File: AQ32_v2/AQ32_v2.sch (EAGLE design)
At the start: 114 parts, among them Q2 BCV27, Q3 BCV27, Q5 BCV27, Q6 BCV27, U1 ITG-3200, U10 MS5611, U11 MIC5239, U13 74AHC1G86DCK, U2 STM32F10XVXT6, U7 USD-SOCKETNEW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

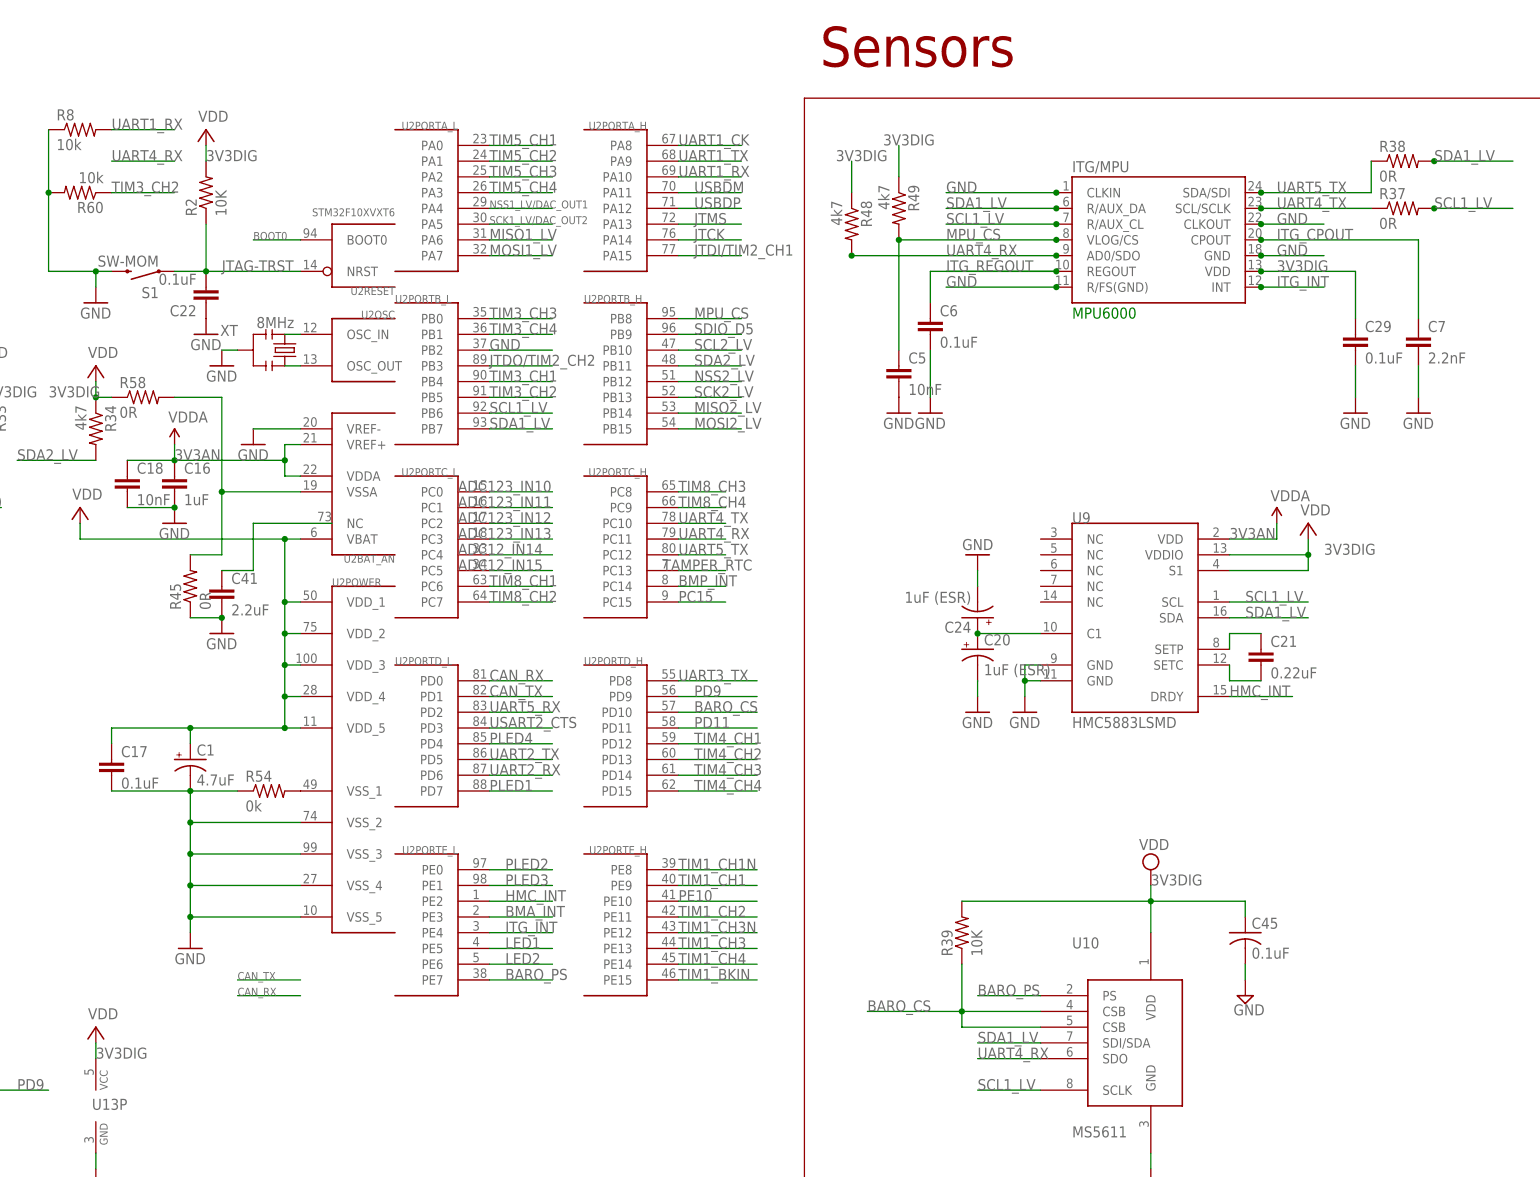
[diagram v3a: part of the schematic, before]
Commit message: converted baro back to using I2C, renamed TX4/TX5 to use I2C3 labels
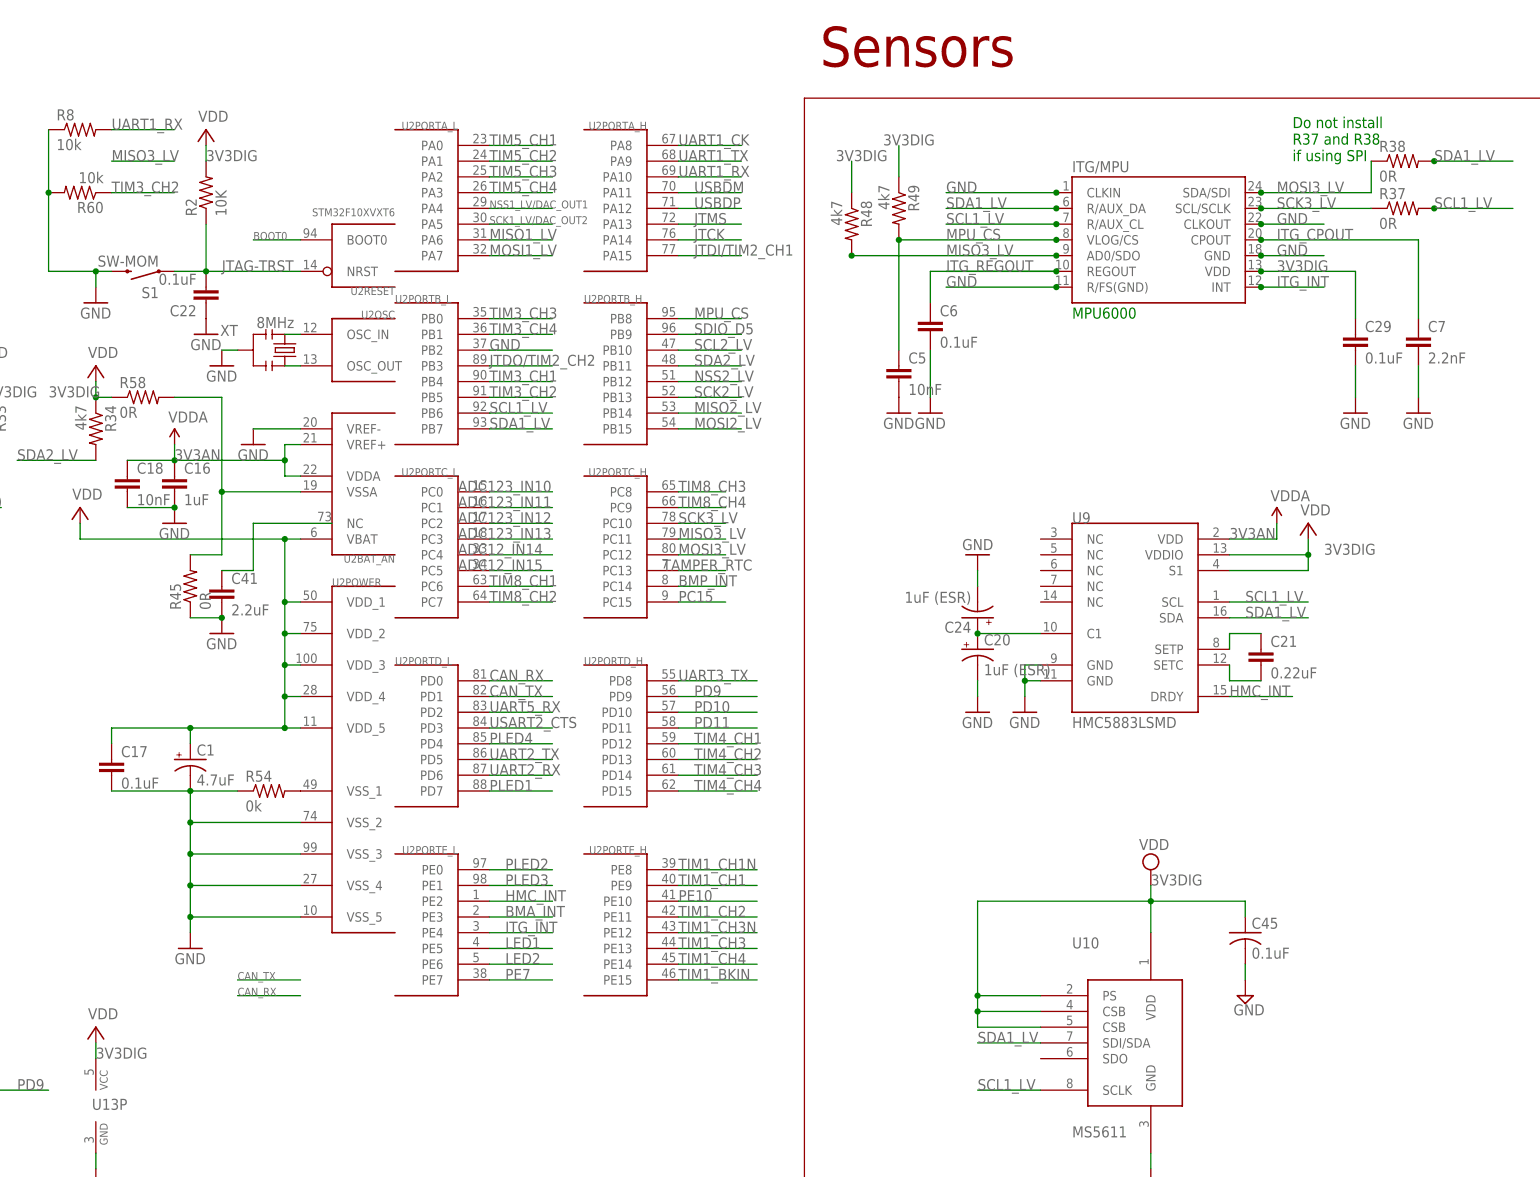
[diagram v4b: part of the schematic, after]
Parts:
- removed R39: 10K, SparkFun:RESISTOR0402
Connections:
- net UART4_TX renamed SCK3_LV
- net UART5_TX renamed MOSI3_LV
- removed net BARO_CS: R39.1, U10.CSB, U10.CSB@2, U2PORTD_H.PD10
- removed net BARO_PS: U10.PS, U2PORTE_L.PE7
- removed net UART4_RX: R48.2, U1.AD0/SDO, U10.SDO, U2PORTC_H.PC11
- new net MISO3_LV: R48.2, U1.AD0/SDO, U2PORTC_H.PC11
- new net PD10: U2PORTD_H.PD10
- new net PE7: U2PORTE_L.PE7
- net 3V3DIG: now also U10.CSB, U10.CSB@2, U10.PS; no longer R39.2
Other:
- note added: "Do not install R37 and R38 if using SPI"
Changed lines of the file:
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@@
 <part name="JP3-1" library="SparkFun-Connectors" deviceset="M09" device=""/>
 <part name="JP3-2" library="SparkFun-Connectors" deviceset="M09" device=""/>
-<part name="R39" library="SparkFun" deviceset="RESISTOR" device="0402" value="10K"/>
 <part name="JP5" library="SparkFun-Connectors" deviceset="M02" device="PTH"/>
 </parts>
@@
 <text x="500.38" y="73.66" size="1.778" layer="91">AI4</text>
 <text x="500.38" y="76.2" size="1.778" layer="91">AI5</text>
+<text x="332.74" y="175.26" size="1.778" layer="91">Do not install
+R37 and R38
+if using SPI</text>
 </plain>
 <instances>
@@
 <instance part="JP3-1" gate="G$1" x="447.04" y="68.58"/>
 <instance part="JP3-2" gate="G$1" x="472.44" y="68.58"/>
-<instance part="R39" gate="G$1" x="279.4" y="50.8" rot="R90"/>
 <instance part="JP5" gate="G$1" x="114.3" y="-43.18"/>
 </instances>
@@
 <wire x1="309.88" y1="58.42" x2="309.88" y2="55.88" width="0.1524" layer="91"/>
 <wire x1="309.88" y1="55.88" x2="309.88" y2="50.8" width="0.1524" layer="91"/>
-<wire x1="279.4" y1="55.88" x2="309.88" y2="55.88" width="0.1524" layer="91"/>
 <wire x1="309.88" y1="55.88" x2="325.12" y2="55.88" width="0.1524" layer="91"/>
 <wire x1="325.12" y1="55.88" x2="325.12" y2="53.34" width="0.1524" layer="91"/>
@@
 <pinref part="C45" gate="G$1" pin="1"/>
 <label x="309.88" y="58.42" size="1.778" layer="95"/>
-<pinref part="R39" gate="G$1" pin="2"/>
+<wire x1="309.88" y1="55.88" x2="281.94" y2="55.88" width="0.1524" layer="91"/>
+<wire x1="281.94" y1="55.88" x2="281.94" y2="40.64" width="0.1524" layer="91"/>
+<pinref part="U10" gate="G$1" pin="CSB@2"/>
+<wire x1="281.94" y1="40.64" x2="281.94" y2="38.1" width="0.1524" layer="91"/>
+<wire x1="281.94" y1="38.1" x2="281.94" y2="35.56" width="0.1524" layer="91"/>
+<wire x1="281.94" y1="35.56" x2="292.1" y2="35.56" width="0.1524" layer="91"/>
+<pinref part="U10" gate="G$1" pin="CSB"/>
+<wire x1="292.1" y1="38.1" x2="281.94" y2="38.1" width="0.1524" layer="91"/>
+<pinref part="U10" gate="G$1" pin="PS"/>
+<wire x1="292.1" y1="40.64" x2="281.94" y2="40.64" width="0.1524" layer="91"/>
+<junction x="281.94" y="40.64"/>
+<junction x="281.94" y="38.1"/>
 </segment>
 <segment>
@@
 </segment>
 </net>
-<net name="UART4_TX" class="0">
+<net name="SCK3_LV" class="0">
 <segment>
 <wire x1="233.68" y1="116.84" x2="241.3" y2="116.84" width="0.1524" layer="91"/>
@@
 </segment>
 </net>
-<net name="UART4_RX" class="0">
+<net name="MISO3_LV" class="0">
 <segment>
 <wire x1="233.68" y1="114.3" x2="241.3" y2="114.3" width="0.1524" layer="91"/>
@@
 <pinref part="U1" gate="G$1" pin="AD0/SDO"/>
 <pinref part="R48" gate="G$1" pin="2"/>
-</segment>
-<segment>
-<pinref part="U10" gate="G$1" pin="SDO"/>
-<wire x1="292.1" y1="30.48" x2="281.94" y2="30.48" width="0.1524" layer="91"/>
-<label x="281.94" y="30.48" size="1.778" layer="95"/>
 </segment>
 </net>
@@
 </segment>
 </net>
-<net name="UART5_TX" class="0">
+<net name="MOSI3_LV" class="0">
 <segment>
 <wire x1="233.68" y1="111.76" x2="241.3" y2="111.76" width="0.1524" layer="91"/>
@@
 </segment>
 </net>
-<net name="BARO_CS" class="0">
+<net name="PD10" class="0">
 <segment>
 <wire x1="233.68" y1="86.36" x2="246.38" y2="86.36" width="0.1524" layer="91"/>
 <label x="236.22" y="86.36" size="1.778" layer="95"/>
 <pinref part="U2" gate="PORTD_H" pin="PD10"/>
-</segment>
-<segment>
-<pinref part="U10" gate="G$1" pin="CSB@2"/>
-<wire x1="292.1" y1="35.56" x2="279.4" y2="35.56" width="0.1524" layer="91"/>
-<pinref part="R39" gate="G$1" pin="1"/>
-<wire x1="279.4" y1="35.56" x2="279.4" y2="38.1" width="0.1524" layer="91"/>
-<pinref part="U10" gate="G$1" pin="CSB"/>
-<wire x1="279.4" y1="38.1" x2="279.4" y2="45.72" width="0.1524" layer="91"/>
-<wire x1="292.1" y1="38.1" x2="279.4" y2="38.1" width="0.1524" layer="91"/>
-<junction x="279.4" y="38.1"/>
-<wire x1="279.4" y1="38.1" x2="264.16" y2="38.1" width="0.1524" layer="91"/>
-<label x="264.16" y="38.1" size="1.778" layer="95"/>
 </segment>
 </net>
@@
 </segment>
 </net>
-<net name="BARO_PS" class="0">
+<net name="PE7" class="0">
 <segment>
 <wire x1="203.2" y1="43.18" x2="213.36" y2="43.18" width="0.1524" layer="91"/>
 <label x="205.74" y="43.18" size="1.778" layer="95"/>
 <pinref part="U2" gate="PORTE_L" pin="PE7"/>
-</segment>
-<segment>
-<pinref part="U10" gate="G$1" pin="PS"/>
-<wire x1="292.1" y1="40.64" x2="281.94" y2="40.64" width="0.1524" layer="91"/>
-<label x="281.94" y="40.64" size="1.778" layer="95"/>
 </segment>
 </net>
@@
 </schematic>
 </drawing>
+<compatibility>
+<note version="6.3" minversion="6.2.2" severity="warning">
+Since Version 6.2.2 text objects can contain more than one line,
+which will not be processed correctly with this version.
+</note>
+</compatibility>
 </eagle>

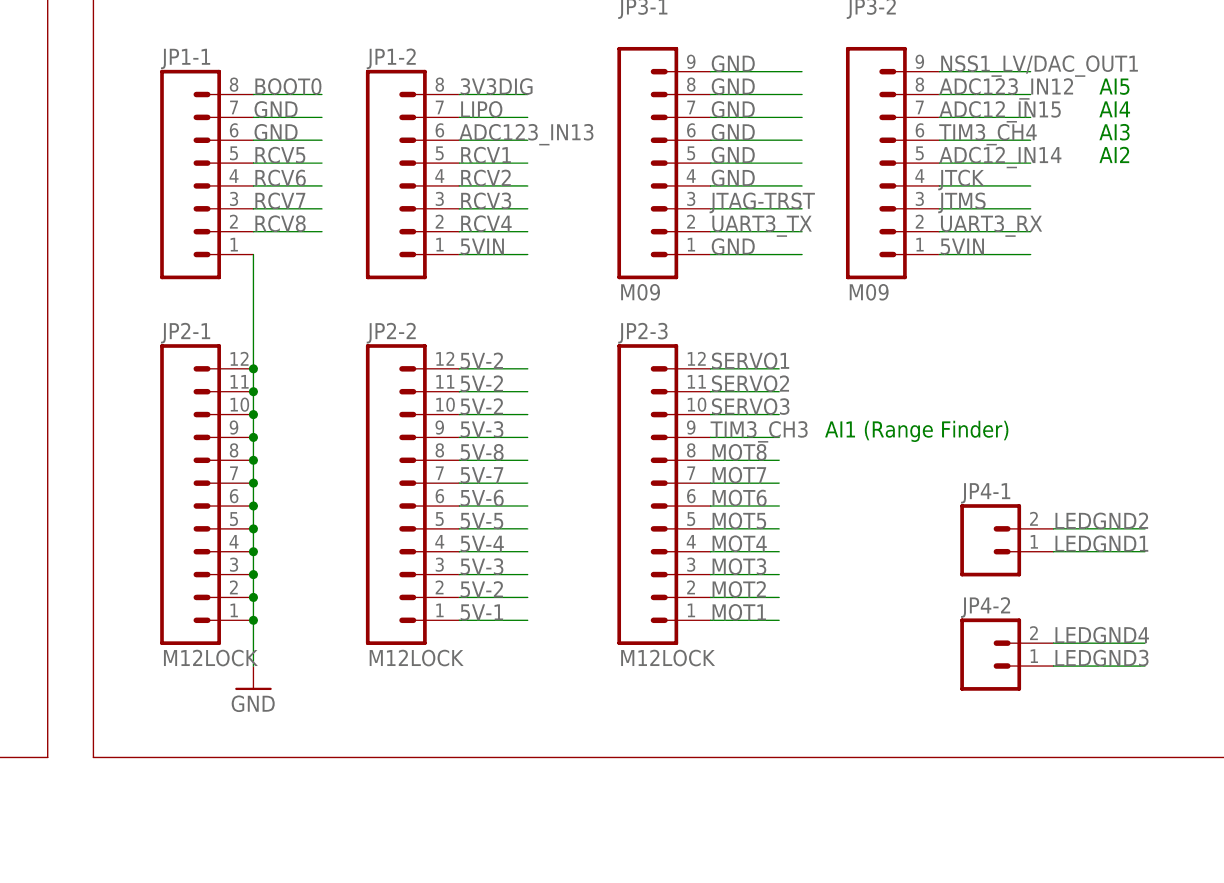
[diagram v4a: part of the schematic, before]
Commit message: fixed airwires
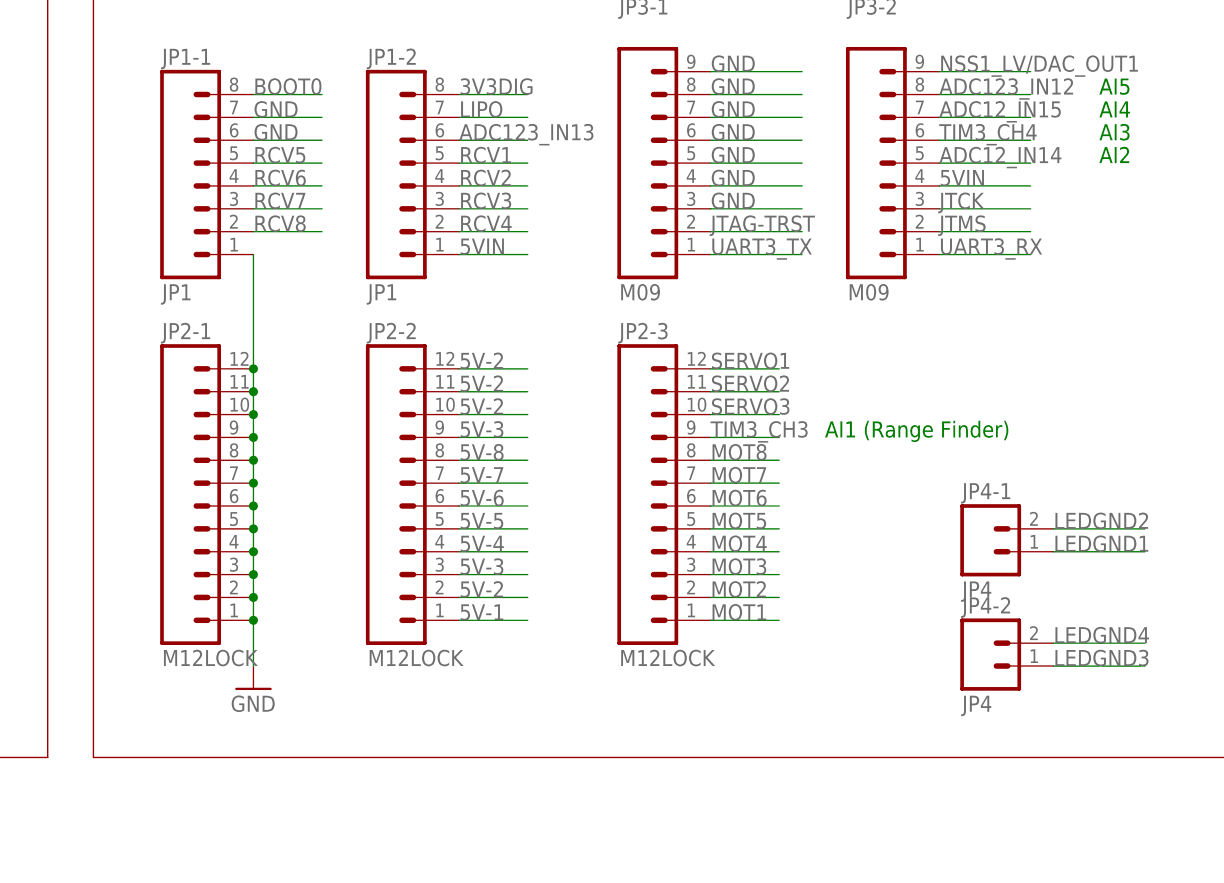
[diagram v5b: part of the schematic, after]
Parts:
- JP1-1, JP1-2: value (none) -> JP1
- JP4-1, JP4-2: value (none) -> JP4
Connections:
- net 5VIN: now also JP3-2.4; no longer JP3-2.1
- net GND: now also JP3-1.3; no longer JP3-1.1
- net JTAG-TRST: now also JP3-1.2; no longer JP3-1.3
- net JTCK: now also JP3-2.3; no longer JP3-2.4
- net JTMS: now also JP3-2.2; no longer JP3-2.3
- net UART3_RX: now also JP3-2.1; no longer JP3-2.2
- net UART3_TX: now also JP3-1.1; no longer JP3-1.2
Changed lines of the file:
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@@
 <part name="GND52" library="SparkFun" deviceset="GND" device=""/>
 <part name="R64" library="SparkFun" deviceset="RESISTOR" device="0402" value="10K"/>
-<part name="JP1-1" library="SparkFun-Connectors" deviceset="M08" device="LOCK"/>
-<part name="JP1-2" library="SparkFun-Connectors" deviceset="M08" device="LOCK"/>
+<part name="JP1-1" library="SparkFun-Connectors" deviceset="M08" device="LOCK" value="JP1"/>
+<part name="JP1-2" library="SparkFun-Connectors" deviceset="M08" device="LOCK" value="JP1"/>
 <part name="JP2-1" library="SparkFun-Connectors" deviceset="M12" device="LOCK"/>
 <part name="JP2-2" library="SparkFun-Connectors" deviceset="M12" device="LOCK"/>
@@
 <part name="OSD" library="con-jst2" deviceset="?M07B-SRSS-TB" device="S"/>
 <part name="L2" library="SparkFun" deviceset="INDUCTOR" device="0805" value="22uH"/>
-<part name="JP4-1" library="SparkFun-Connectors" deviceset="M02" device="LOCK"/>
-<part name="JP4-2" library="SparkFun-Connectors" deviceset="M02" device="LOCK"/>
+<part name="JP4-1" library="SparkFun-Connectors" deviceset="M02" device="LOCK" value="JP4"/>
+<part name="JP4-2" library="SparkFun-Connectors" deviceset="M02" device="LOCK" value="JP4"/>
 <part name="JP3-1" library="SparkFun-Connectors" deviceset="M09" device=""/>
 <part name="JP3-2" library="SparkFun-Connectors" deviceset="M09" device=""/>
@@
 </segment>
 <segment>
-<pinref part="JP3-1" gate="G$1" pin="1"/>
-<wire x1="457.2" y1="58.42" x2="467.36" y2="58.42" width="0.1524" layer="91"/>
-<label x="457.2" y="58.42" size="1.778" layer="95"/>
-</segment>
-<segment>
 <pinref part="JP3-1" gate="G$1" pin="5"/>
 <wire x1="457.2" y1="68.58" x2="467.36" y2="68.58" width="0.1524" layer="91"/>
@@
 <wire x1="457.2" y1="78.74" x2="467.36" y2="78.74" width="0.1524" layer="91"/>
 <label x="457.2" y="78.74" size="1.778" layer="95"/>
+</segment>
+<segment>
+<pinref part="JP3-1" gate="G$1" pin="3"/>
+<wire x1="457.2" y1="63.5" x2="467.36" y2="63.5" width="0.1524" layer="91"/>
+<label x="457.2" y="63.5" size="1.778" layer="95"/>
 </segment>
 </net>
@@
 </segment>
 <segment>
-<pinref part="JP3-2" gate="G$1" pin="1"/>
-<wire x1="482.6" y1="58.42" x2="492.76" y2="58.42" width="0.1524" layer="91"/>
-<label x="482.6" y="58.42" size="1.778" layer="95"/>
+<pinref part="JP3-2" gate="G$1" pin="4"/>
+<wire x1="482.6" y1="66.04" x2="492.76" y2="66.04" width="0.1524" layer="91"/>
+<label x="482.6" y="66.04" size="1.778" layer="95"/>
 </segment>
 </net>
@@
 </segment>
 <segment>
-<pinref part="JP3-1" gate="G$1" pin="3"/>
-<wire x1="457.2" y1="63.5" x2="467.36" y2="63.5" width="0.1524" layer="91"/>
-<label x="457.2" y="63.5" size="1.778" layer="95"/>
+<pinref part="JP3-1" gate="G$1" pin="2"/>
+<wire x1="457.2" y1="60.96" x2="467.36" y2="60.96" width="0.1524" layer="91"/>
+<label x="457.2" y="60.96" size="1.778" layer="95"/>
 </segment>
 </net>
@@
 </segment>
 <segment>
-<pinref part="JP3-1" gate="G$1" pin="2"/>
-<wire x1="457.2" y1="60.96" x2="467.36" y2="60.96" width="0.1524" layer="91"/>
-<label x="457.2" y="60.96" size="1.778" layer="95"/>
+<pinref part="JP3-1" gate="G$1" pin="1"/>
+<wire x1="457.2" y1="58.42" x2="467.36" y2="58.42" width="0.1524" layer="91"/>
+<label x="457.2" y="58.42" size="1.778" layer="95"/>
 </segment>
 </net>
@@
 </segment>
 <segment>
-<pinref part="JP3-2" gate="G$1" pin="2"/>
-<wire x1="482.6" y1="60.96" x2="492.76" y2="60.96" width="0.1524" layer="91"/>
-<label x="482.6" y="60.96" size="1.778" layer="95"/>
+<pinref part="JP3-2" gate="G$1" pin="1"/>
+<wire x1="482.6" y1="58.42" x2="492.76" y2="58.42" width="0.1524" layer="91"/>
+<label x="482.6" y="58.42" size="1.778" layer="95"/>
 </segment>
 </net>
@@
 </segment>
 <segment>
-<pinref part="JP3-2" gate="G$1" pin="4"/>
-<wire x1="482.6" y1="66.04" x2="492.76" y2="66.04" width="0.1524" layer="91"/>
-<label x="482.6" y="66.04" size="1.778" layer="95"/>
+<pinref part="JP3-2" gate="G$1" pin="3"/>
+<wire x1="482.6" y1="63.5" x2="492.76" y2="63.5" width="0.1524" layer="91"/>
+<label x="482.6" y="63.5" size="1.778" layer="95"/>
 </segment>
 </net>
@@
 </segment>
 <segment>
-<pinref part="JP3-2" gate="G$1" pin="3"/>
-<wire x1="482.6" y1="63.5" x2="492.76" y2="63.5" width="0.1524" layer="91"/>
-<label x="482.6" y="63.5" size="1.778" layer="95"/>
-</segment>
-</net>
+<pinref part="JP3-2" gate="G$1" pin="2"/>
+<wire x1="482.6" y1="60.96" x2="492.76" y2="60.96" width="0.1524" layer="91"/>
+<label x="482.6" y="60.96" size="1.778" layer="95"/>
+</segment>
+</net>
